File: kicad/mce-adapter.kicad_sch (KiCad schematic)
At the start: 20 parts, among them J1 Conn_02x02_Odd_Even, J2 Conn_01x03_Male, U1 GAL16V8B

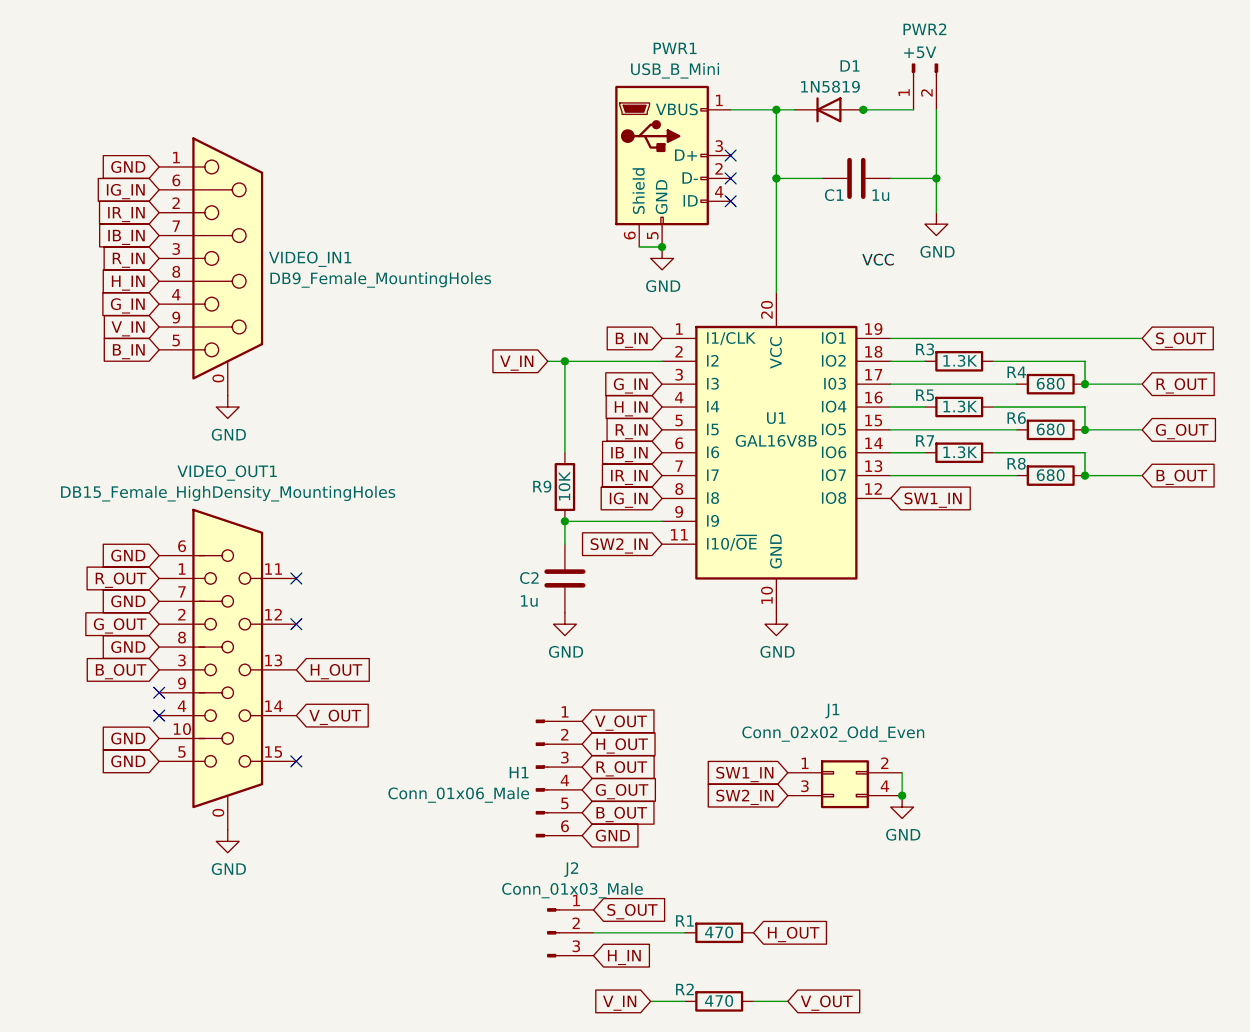
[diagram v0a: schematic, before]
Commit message: fix: replace C2 with 4,7uF
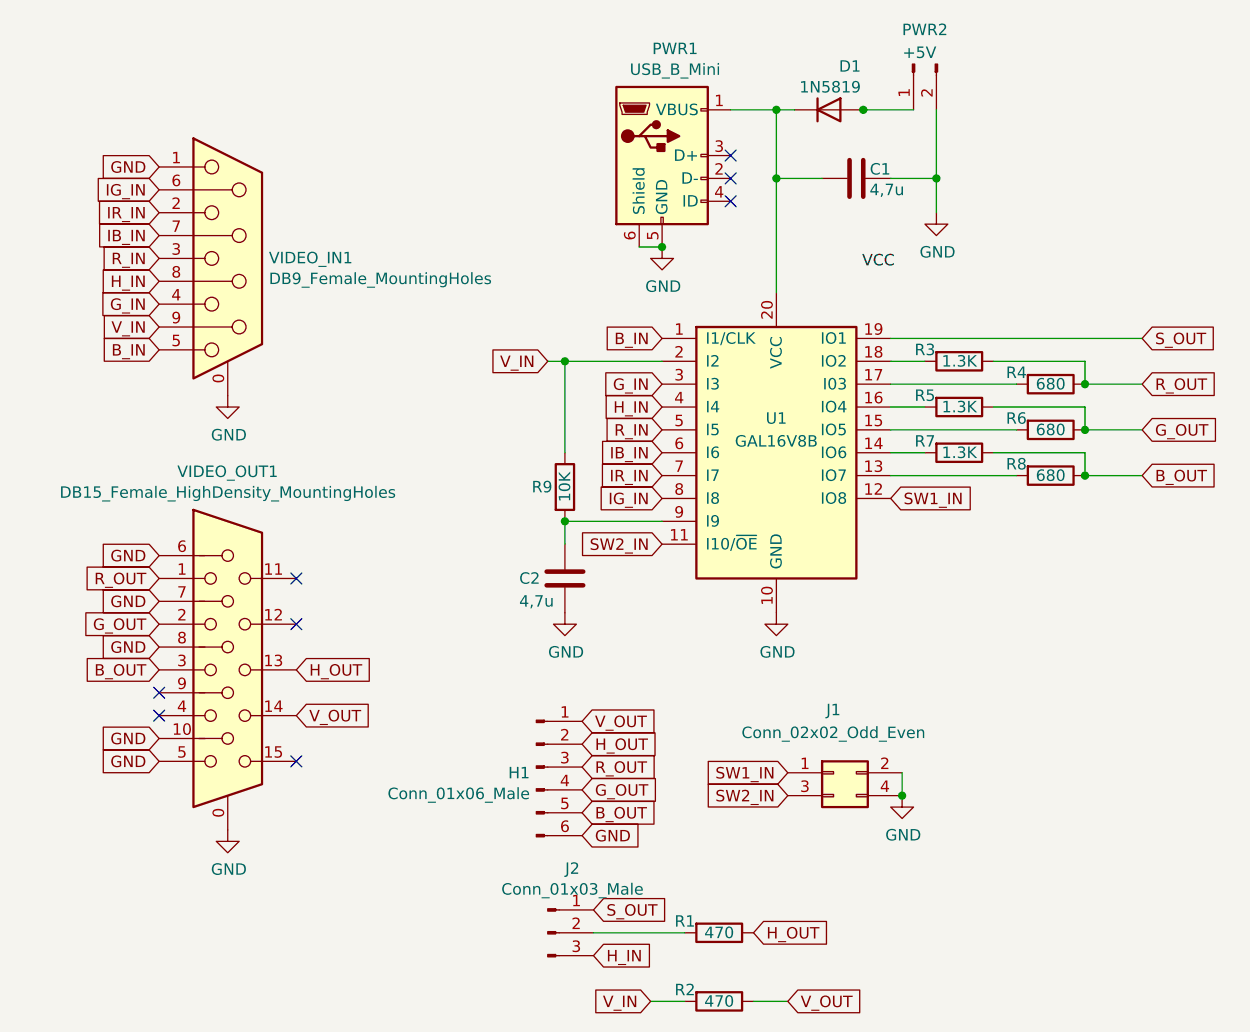
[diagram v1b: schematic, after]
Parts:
- C1, C2: value 1u -> 4,7u; LCSC C2839237 -> C472888
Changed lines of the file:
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@@
 	(title_block
 		(title "MCE Adapter")
-		(date "2024-02-13")
-		(rev "0.10.1")
+		(date "2025-02-04")
+		(rev "0.10.2")
 		(company "Necroware")
 		(comment 1 "by Scorp")
@@
 	(label "VCC"
 		(at 113.665 46.99 0)
-		(fields_autoplaced yes)
 		(effects
 			(font
@@
 			)
 		)
-		(property "Datasheet" " ~"
+		(property "Datasheet" "~"
 			(at 19.05 81.28 0)
 			(effects
@@
 			)
 		)
-		(property "Datasheet" " ~"
+		(property "Datasheet" "~"
 			(at 43.18 45.72 0)
 			(effects
@@
 			)
 		)
-		(property "Value" "1u"
+		(property "Value" "4,7u"
 			(at 75.565 83.82 0)
 			(effects
@@
 			)
 		)
-		(property "LCSC" "C2839237"
+		(property "LCSC" " C472888"
 			(at 80.645 81.28 0)
 			(effects
@@
 		(dnp no)
 		(property "Reference" "C1"
-			(at 111.76 38.735 90)
+			(at 116.84 35.814 90)
 			(effects
 				(font
@@
 			)
 		)
-		(property "Value" "1u"
-			(at 116.84 38.735 90)
+		(property "Value" "4,7u"
+			(at 118.364 38.1 90)
 			(effects
 				(font
@@
 			)
 		)
-		(property "LCSC" "C2839237"
+		(property "LCSC" " C472888"
 			(at 113.03 36.83 0)
 			(effects

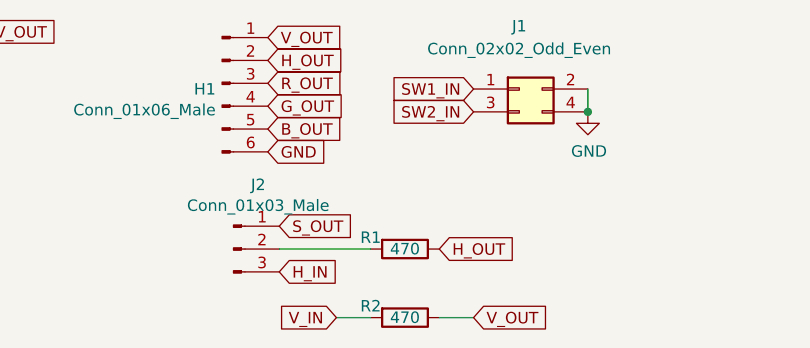
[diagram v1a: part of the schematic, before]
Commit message: issue-15: reduce resistor values
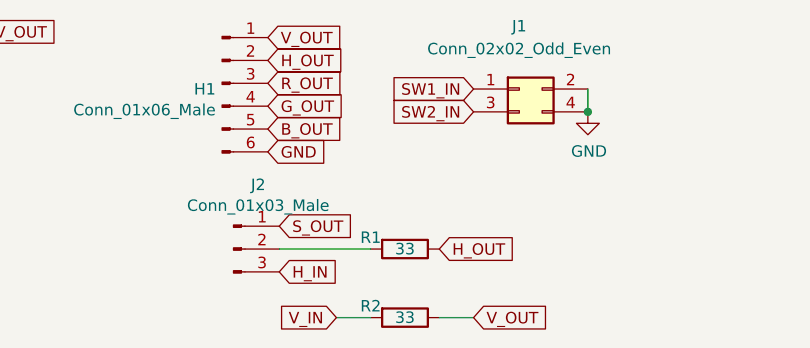
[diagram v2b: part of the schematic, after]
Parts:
- R1, R2: value 470 -> 33; LCSC C119317 -> C713968
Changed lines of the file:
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@@
 	(title_block
 		(title "MCE Adapter")
-		(date "2025-02-04")
+		(date "2025-02-09")
 		(rev "0.10.2")
 		(company "Necroware")
@@
 			)
 		)
-		(property "Value" "470"
+		(property "Value" "33"
 			(at 97.79 120.65 90)
 			(effects
@@
 			)
 		)
-		(property "LCSC" "C119317"
+		(property "LCSC" "C713968"
 			(at 97.79 120.65 0)
 			(effects
@@
 			)
 		)
-		(property "Value" "470"
+		(property "Value" "33"
 			(at 97.79 128.27 90)
 			(effects
@@
 			)
 		)
-		(property "LCSC" "C119317"
+		(property "LCSC" "C713968"
 			(at 97.79 128.27 0)
 			(effects
